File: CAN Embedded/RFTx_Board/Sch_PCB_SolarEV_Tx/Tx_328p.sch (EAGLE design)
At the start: 4 parts, among them U2 ATMEGA328P_PDIP

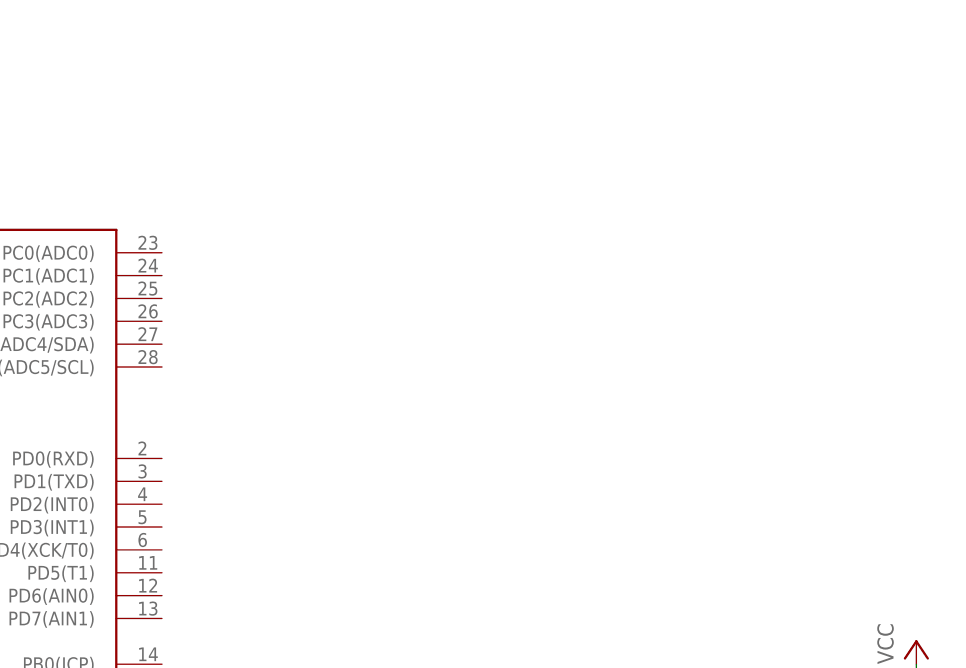
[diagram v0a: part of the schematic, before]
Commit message: More EAGLE *Not sure which pin headers? *PDIP or SMD for MCU and if so which layout, as 328p SMD types pinouts seem to differ *Everything needed is connected (i think)
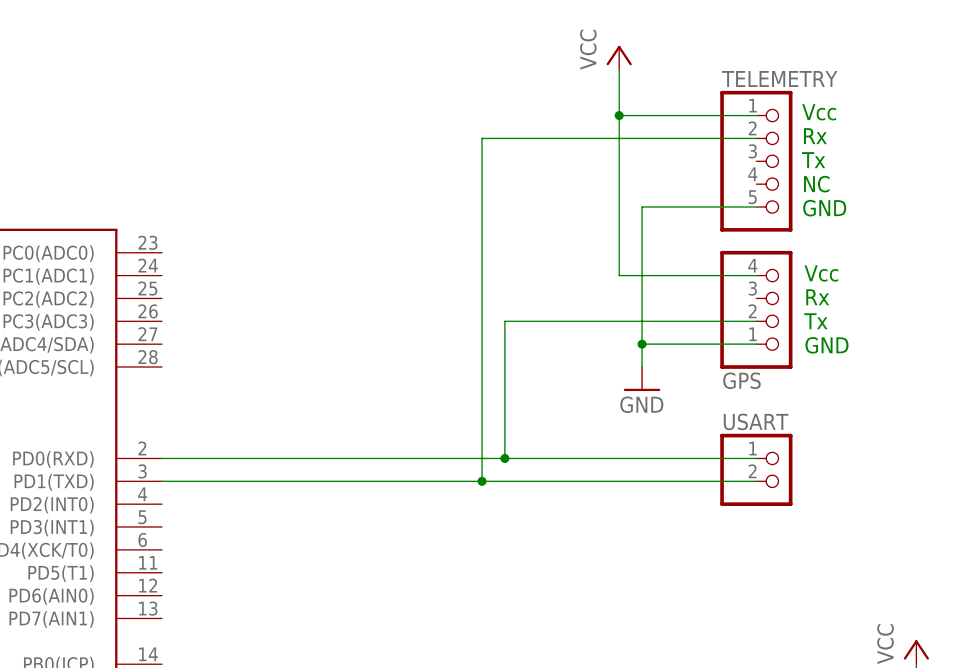
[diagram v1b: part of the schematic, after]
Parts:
- added GPS: (no value), pinhead:PINHD-1X4
- added TELEMETRY: (no value), pinhead:PINHD-1X5
- added USART: (no value), pinhead:PINHD-1X2
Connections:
- new net N$4: GPS.2, U2.PD0(RXD), USART.1
- new net N$8: TELEMETRY.2, U2.PD1(TXD), USART.2
- net GND: now also GPS.1, TELEMETRY.5
- net VCC: now also GPS.4, TELEMETRY.1
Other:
- note added: "Vcc Rx Tx GND"
- note added: "Vcc Rx Tx NC GND"
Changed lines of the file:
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@@
 <setting verticaltext="up"/>
 </settings>
-<grid distance="0.1" unitdist="inch" unit="inch" style="lines" multiple="1" display="no" altdistance="0.01" altunitdist="inch" altunit="inch"/>
+<grid distance="0.1" unitdist="inch" unit="mm" style="lines" multiple="1" display="no" altdistance="0.01" altunitdist="inch" altunit="mm"/>
 <layers>
 <layer number="1" name="Top" color="4" fill="1" visible="no" active="no"/>
@@
 <part name="P+2" library="supply1" deviceset="VCC" device=""/>
 <part name="GND2" library="supply1" deviceset="GND" device=""/>
+<part name="USART" library="pinhead" deviceset="PINHD-1X2" device=""/>
+<part name="GPS" library="pinhead" deviceset="PINHD-1X4" device=""/>
+<part name="P+3" library="supply1" deviceset="VCC" device=""/>
+<part name="GND3" library="supply1" deviceset="GND" device=""/>
+<part name="TELEMETRY" library="pinhead" deviceset="PINHD-1X5" device=""/>
 </parts>
 <sheets>
 <sheet>
 <plain>
+<text x="190.5" y="95.504" size="1.778" layer="91">Vcc
+Rx
+Tx
+NC
+GND</text>
+<text x="190.754" y="80.264" size="1.778" layer="91">Vcc
+Rx
+Tx
+GND</text>
 </plain>
 <instances>
@@
 <instance part="P+2" gate="VCC" x="203.2" y="48.26"/>
 <instance part="GND2" gate="1" x="203.2" y="17.78"/>
+<instance part="USART" gate="G$1" x="187.96" y="66.04"/>
+<instance part="GPS" gate="A" x="187.96" y="86.36" rot="MR180"/>
+<instance part="P+3" gate="VCC" x="170.18" y="114.3"/>
+<instance part="GND3" gate="1" x="172.72" y="76.2"/>
+<instance part="TELEMETRY" gate="A" x="187.96" y="101.6"/>
 </instances>
 <busses>
@@
 <pinref part="SPI_HEADER" gate="A" pin="6"/>
 <wire x1="203.2" y1="33.02" x2="193.04" y2="33.02" width="0.1524" layer="91"/>
+</segment>
+<segment>
+<pinref part="GPS" gate="A" pin="1"/>
+<pinref part="GND3" gate="1" pin="GND"/>
+<wire x1="185.42" y1="81.28" x2="172.72" y2="81.28" width="0.1524" layer="91"/>
+<wire x1="172.72" y1="81.28" x2="172.72" y2="78.74" width="0.1524" layer="91"/>
+<pinref part="TELEMETRY" gate="A" pin="5"/>
+<wire x1="185.42" y1="96.52" x2="172.72" y2="96.52" width="0.1524" layer="91"/>
+<wire x1="172.72" y1="96.52" x2="172.72" y2="81.28" width="0.1524" layer="91"/>
+<junction x="172.72" y="81.28"/>
 </segment>
 </net>
@@
 <wire x1="203.2" y1="38.1" x2="203.2" y2="45.72" width="0.1524" layer="91"/>
 </segment>
+<segment>
+<pinref part="GPS" gate="A" pin="4"/>
+<pinref part="P+3" gate="VCC" pin="VCC"/>
+<wire x1="185.42" y1="88.9" x2="170.18" y2="88.9" width="0.1524" layer="91"/>
+<wire x1="170.18" y1="88.9" x2="170.18" y2="106.68" width="0.1524" layer="91"/>
+<pinref part="TELEMETRY" gate="A" pin="1"/>
+<wire x1="170.18" y1="106.68" x2="170.18" y2="111.76" width="0.1524" layer="91"/>
+<wire x1="185.42" y1="106.68" x2="170.18" y2="106.68" width="0.1524" layer="91"/>
+<junction x="170.18" y="106.68"/>
+</segment>
 </net>
 <net name="N$7" class="0">
@@
 </segment>
 </net>
+<net name="N$4" class="0">
+<segment>
+<pinref part="U2" gate="G$1" pin="PD0(RXD)"/>
+<pinref part="USART" gate="G$1" pin="1"/>
+<wire x1="119.38" y1="68.58" x2="157.48" y2="68.58" width="0.1524" layer="91"/>
+<wire x1="157.48" y1="68.58" x2="185.42" y2="68.58" width="0.1524" layer="91"/>
+<wire x1="157.48" y1="68.58" x2="157.48" y2="83.82" width="0.1524" layer="91"/>
+<pinref part="GPS" gate="A" pin="2"/>
+<wire x1="157.48" y1="83.82" x2="185.42" y2="83.82" width="0.1524" layer="91"/>
+<junction x="157.48" y="68.58"/>
+</segment>
+</net>
+<net name="N$8" class="0">
+<segment>
+<pinref part="U2" gate="G$1" pin="PD1(TXD)"/>
+<pinref part="USART" gate="G$1" pin="2"/>
+<wire x1="119.38" y1="66.04" x2="154.94" y2="66.04" width="0.1524" layer="91"/>
+<pinref part="TELEMETRY" gate="A" pin="2"/>
+<wire x1="154.94" y1="66.04" x2="185.42" y2="66.04" width="0.1524" layer="91"/>
+<wire x1="185.42" y1="104.14" x2="154.94" y2="104.14" width="0.1524" layer="91"/>
+<wire x1="154.94" y1="104.14" x2="154.94" y2="66.04" width="0.1524" layer="91"/>
+<junction x="154.94" y="66.04"/>
+</segment>
+</net>
 </nets>
 </sheet>
@@
 </schematic>
 </drawing>
+<compatibility>
+<note version="6.3" minversion="6.2.2" severity="warning">
+Since Version 6.2.2 text objects can contain more than one line,
+which will not be processed correctly with this version.
+</note>
+</compatibility>
 </eagle>
